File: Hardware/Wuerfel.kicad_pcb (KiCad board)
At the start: 2 copper layers, 17 parts, among them SW1 SW_Push, U1 ATTINY13A-PU

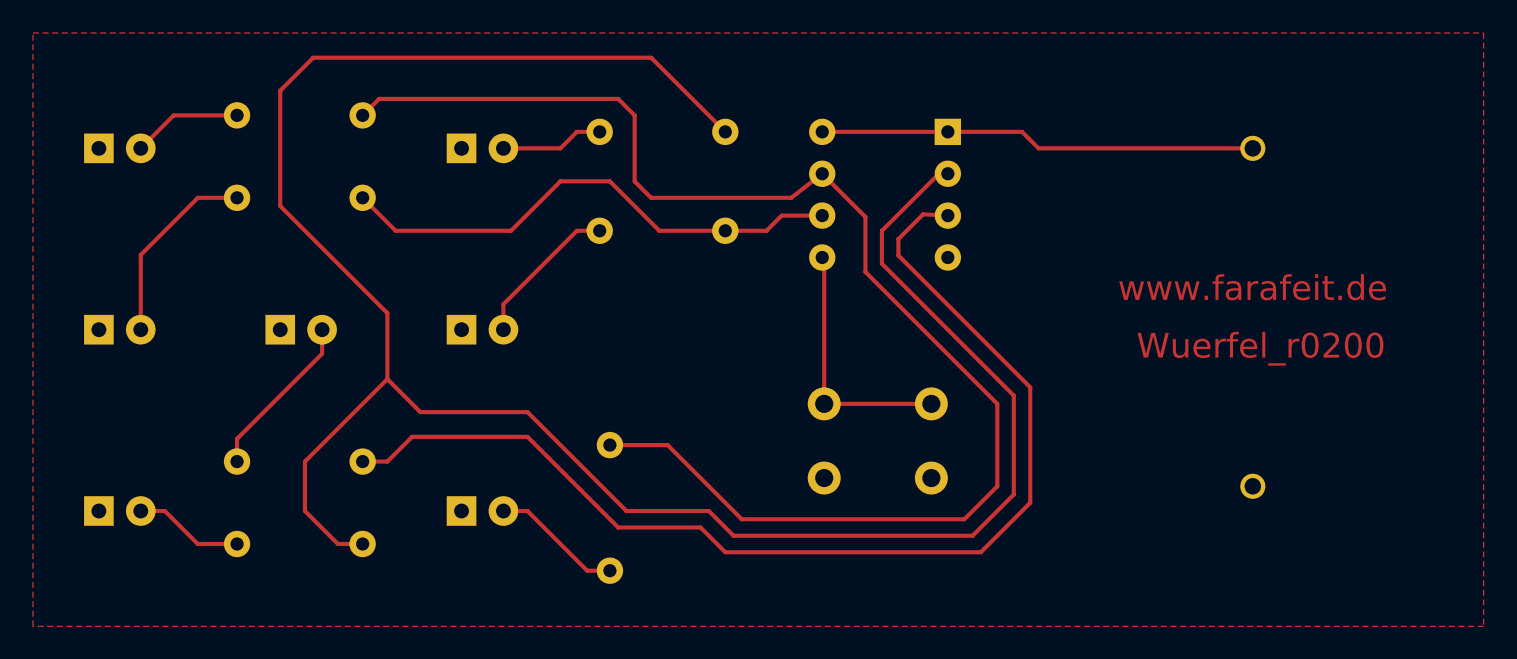
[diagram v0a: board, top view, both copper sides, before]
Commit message: Changed footprint of resistors; re-routing
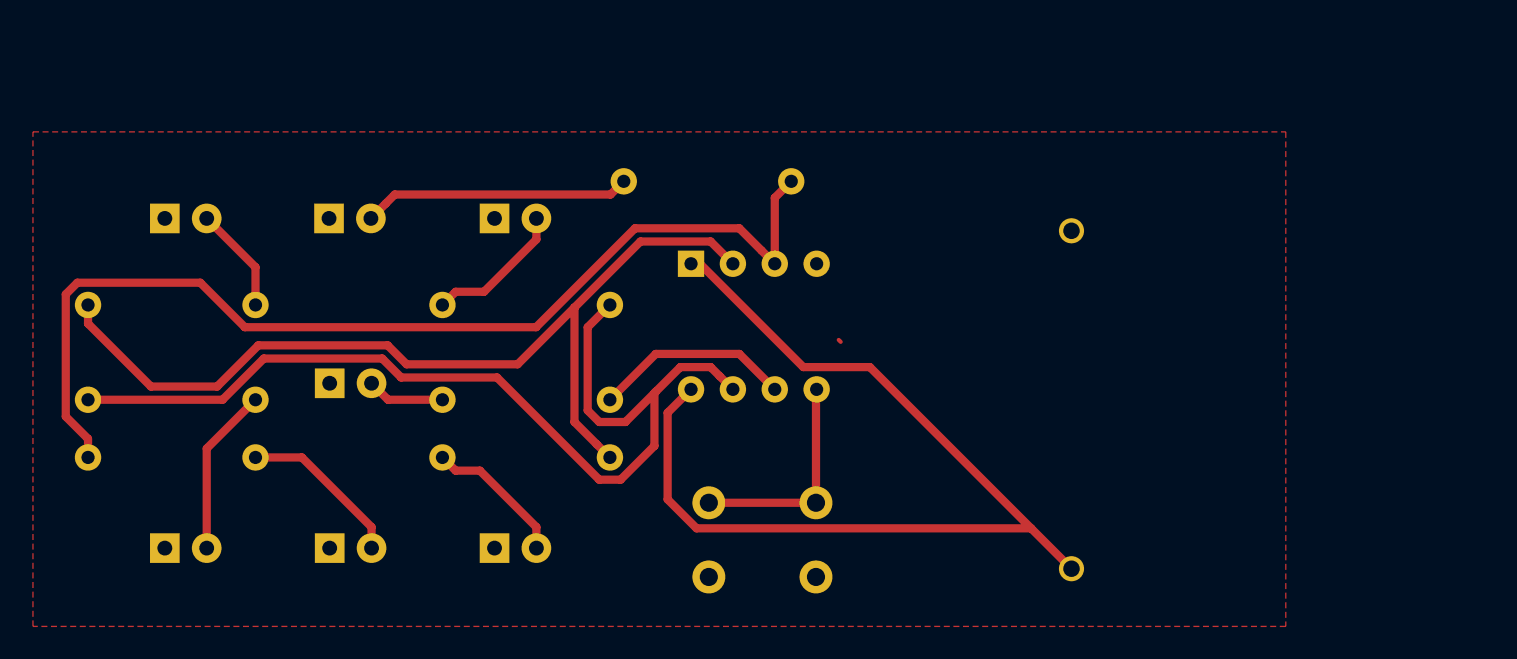
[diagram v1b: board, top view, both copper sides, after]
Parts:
- R1, R2, R3, R4, R5, R6, R7: footprint Resistors_THT:R_Axial_DIN0207_L6.3mm_D2.5mm_P7.62mm_Horizontal -> Resistors_THT:R_Axial_DIN0207_L6.3mm_D2.5mm_P10.16mm_Horizontal
- moved R6 34.1 mm to (166.0, 61.0)
- moved R3 31.8 mm to (123.3, 74.2), turned to 0 degrees
- moved D5 24.3 mm to (148.0, 83.2)
- moved D6 22.6 mm to (138.0, 63.2)
- moved R5 21.0 mm to (155.0, 77.8)
- moved R4 20.2 mm to (123.3, 68.5), turned to 0 degrees
- moved R1 19.4 mm to (155.0, 74.2)
- moved D3 18.1 mm to (128.0, 83.2)
- moved U1 17.5 mm to (159.9, 66.0), turned to 270 degrees
- moved R7 16.7 mm to (123.3, 77.8), turned to 0 degrees
- moved D1 14.4 mm to (138.0, 73.2)
- moved D7 13.6 mm to (138.0, 83.2)
- moved BT1 11.3 mm to (183.0, 70.5), turned to 0 degrees
- moved SW1 9.22 mm to (161.0, 85.0)
- moved R2 8.32 mm to (155.0, 68.5)
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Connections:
- R2 pad 1: Net-(R1-Pad1) -> Net-(R2-Pad1)
- R3 pad 1: Net-(R3-Pad1) -> Net-(R2-Pad1)
- R4 pad 1: Net-(R3-Pad1) -> Net-(R4-Pad1)
- R5 pad 1: Net-(R5-Pad1) -> Net-(R4-Pad1)
- R6 pad 1: Net-(R5-Pad1) -> Net-(R6-Pad1)
- R7 pad 1: Net-(R7-Pad1) -> Net-(R6-Pad1)
- U1 pad 2: Net-(R5-Pad1) -> Net-(R4-Pad1)
- U1 pad 3: Net-(R7-Pad1) -> Net-(R6-Pad1)
- U1 pad 7: Net-(R3-Pad1) -> Net-(R2-Pad1)
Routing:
- net Net-(R5-Pad1): track 132.0 -> 0.00 mm
- net Net-(R3-Pad1): track 83.2 -> 0.00 mm
- net Net-(R7-Pad1): track 68.2 -> 0.00 mm
- net Net-(R6-Pad1): track 0.00 -> 63.7 mm
- net Net-(R2-Pad1): track 0.00 -> 60.6 mm
- net Net-(R4-Pad1): track 0.00 -> 57.0 mm
- net /+3V: track 26.5 -> 60.8 mm
- net Net-(R1-Pad1): track 31.6 -> 12.0 mm
- net Net-(D6-Pad2): track 6.67 -> 16.3 mm
- net Net-(D1-Pad2): track 11.8 -> 5.07 mm
- net Net-(D5-Pad2): track 6.25 -> 9.27 mm
- net Net-(D3-Pad2): track 7.96 -> 10.2 mm
- net Net-(SW1-Pad2): track 15.4 -> 13.4 mm
- net Net-(D2-Pad2): track 9.23 -> 8.67 mm
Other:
- net class Default: clearance 0.2 -> 0.3; trace_width 0.25 -> 0.5
- net class Power added: clearance 0.3, trace_width 1, via_dia 0.6, via_drill 0.4
- rule trace_clearance: 0.2 -> 0.3
- board text added: "Wuerfel_r0102"
- board text removed: "Wuerfel_r0200"
